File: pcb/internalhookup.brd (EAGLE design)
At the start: 29.6 x 16.9 mm, 8 parts, among them CN1 LASER, J1 CONTROL, J2 SERVO, J4 AZIMUTH, Q2 SMMBT2222ALT, U1 AMS1117-3.3

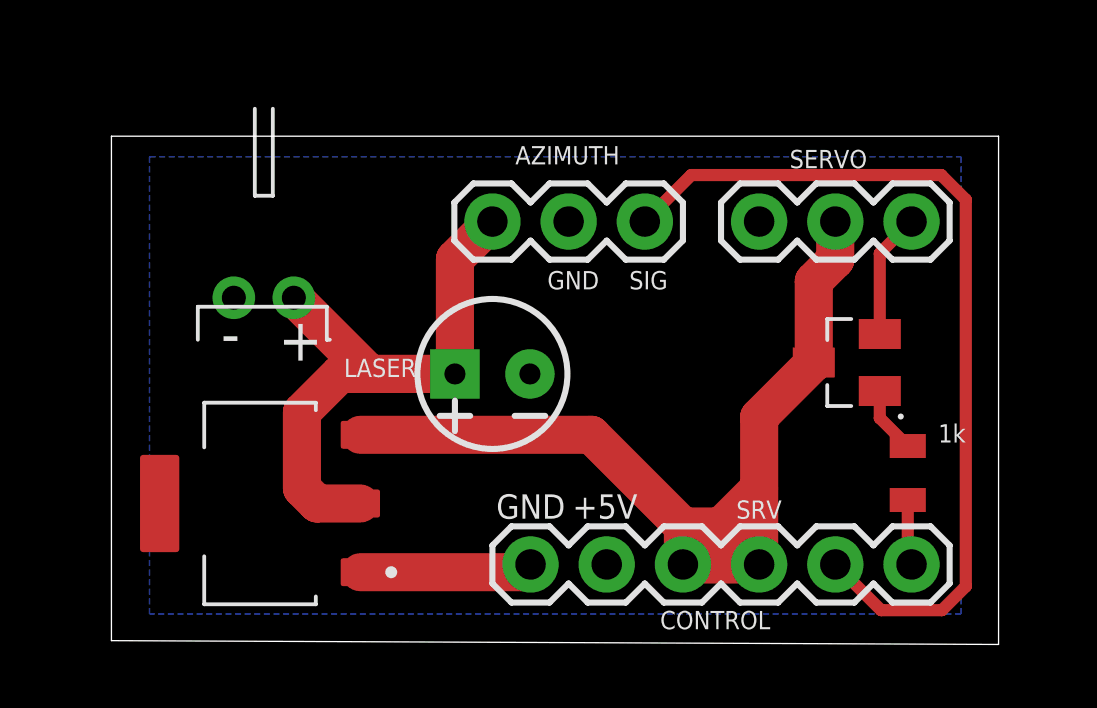
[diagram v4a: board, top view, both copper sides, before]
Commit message: PCB fixups
* Bumped PCB revisions
* Layout changes and some silk screen updates
* No functionality changes
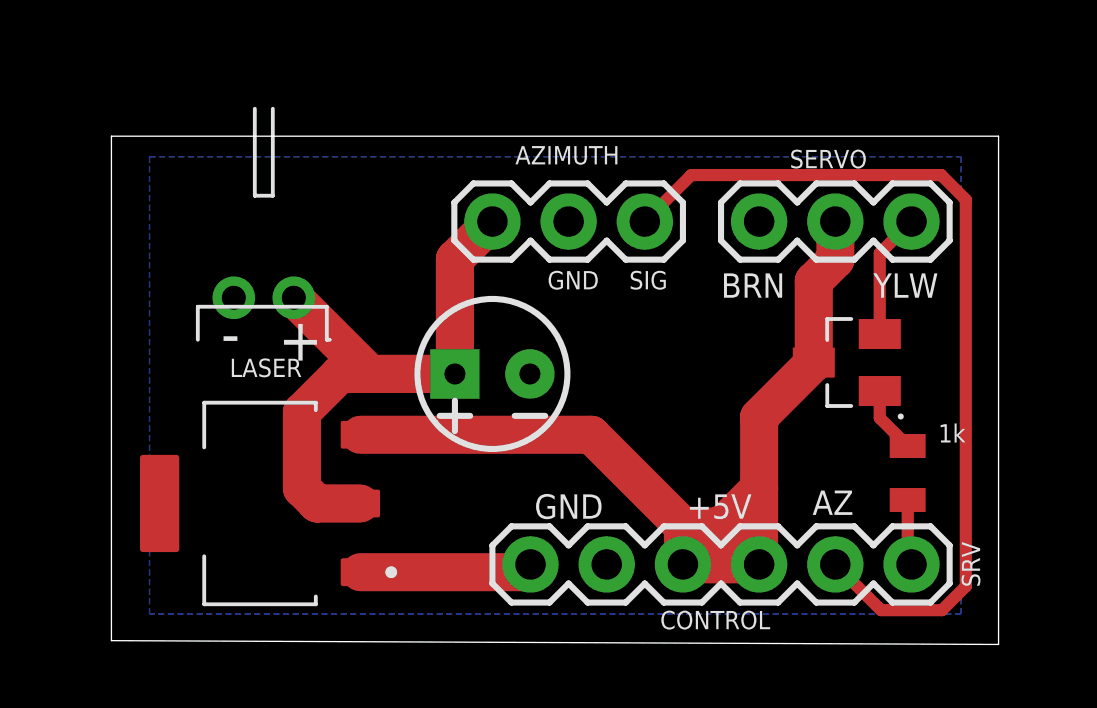
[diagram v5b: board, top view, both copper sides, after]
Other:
- board text added: "AZ"
- board text added: "BRN"
- board text added: "YLW"
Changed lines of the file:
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@@
 <wire x1="29.571" y1="16.815" x2="0" y2="16.815" width="0" layer="20"/>
 <wire x1="0" y1="16.815" x2="0" y2="0" width="0" layer="20"/>
-<text x="15.367" y="4.064" size="0.8128" layer="121">+5V</text>
-<text x="12.827" y="4.064" size="0.8128" layer="121">GND</text>
+<text x="19.177" y="4.064" size="0.8128" layer="121">+5V</text>
+<text x="14.097" y="4.064" size="0.8128" layer="121">GND</text>
 <text x="22.606" y="15.748" size="0.6096" layer="121">SERVO</text>
 <text x="18.288" y="0.381" size="0.6096" layer="121">CONTROL</text>
 <text x="27.559" y="6.604" size="0.6096" layer="121">1k</text>
-<text x="10.16" y="9.398" size="0.6096" layer="121" rot="R180">LASER</text>
+<text x="6.35" y="9.398" size="0.6096" layer="121" rot="R180">LASER</text>
 <text x="16.256" y="12.319" size="0.6096" layer="121" rot="R180">GND</text>
 <text x="18.542" y="12.319" size="0.6096" layer="121" rot="R180">SIG</text>
@@
 February 2021
 Version 1.4</text>
-<text x="20.828" y="4.064" size="0.6096" layer="121">SRV</text>
+<text x="28.956" y="1.778" size="0.6096" layer="121" rot="R90">SRV</text>
 <text x="13.462" y="15.875" size="0.6096" layer="121">AZIMUTH</text>
+<text x="23.368" y="4.191" size="0.8128" layer="121">AZ</text>
+<text x="20.32" y="11.43" size="0.8128" layer="121">BRN</text>
+<text x="25.4" y="11.43" size="0.8128" layer="121">YLW</text>
 </plain>
 <attributes>
@@
 <attribute name="PROD_ID" value="CONN-08437" x="26.67" y="2.54" size="0.8128" layer="27" rot="R180" display="off"/>
 </element>
-<element name="J4" library="SparkFun-Connectors" library_urn="urn:adsk.eagle:library:513" package="1X03" package3d_urn="urn:adsk.eagle:package:38063/1" value="AZIMUTH" x="12.7" y="13.97" smashed="yes">
-<attribute name="VALUE" x="11.43" y="11.938" size="0.6096" layer="27" font="vector" ratio="20"/>
-</element>
+<element name="J4" library="SparkFun-Connectors" library_urn="urn:adsk.eagle:library:513" package="1X03" package3d_urn="urn:adsk.eagle:package:38063/1" value="AZIMUTH" x="12.7" y="13.97" smashed="yes"/>
 </elements>
 <signals>

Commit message: Hookup board revision to 1.6
* Added a cap in front of the servo as the line to get the 5V is long
and may not be totally reliable under stress
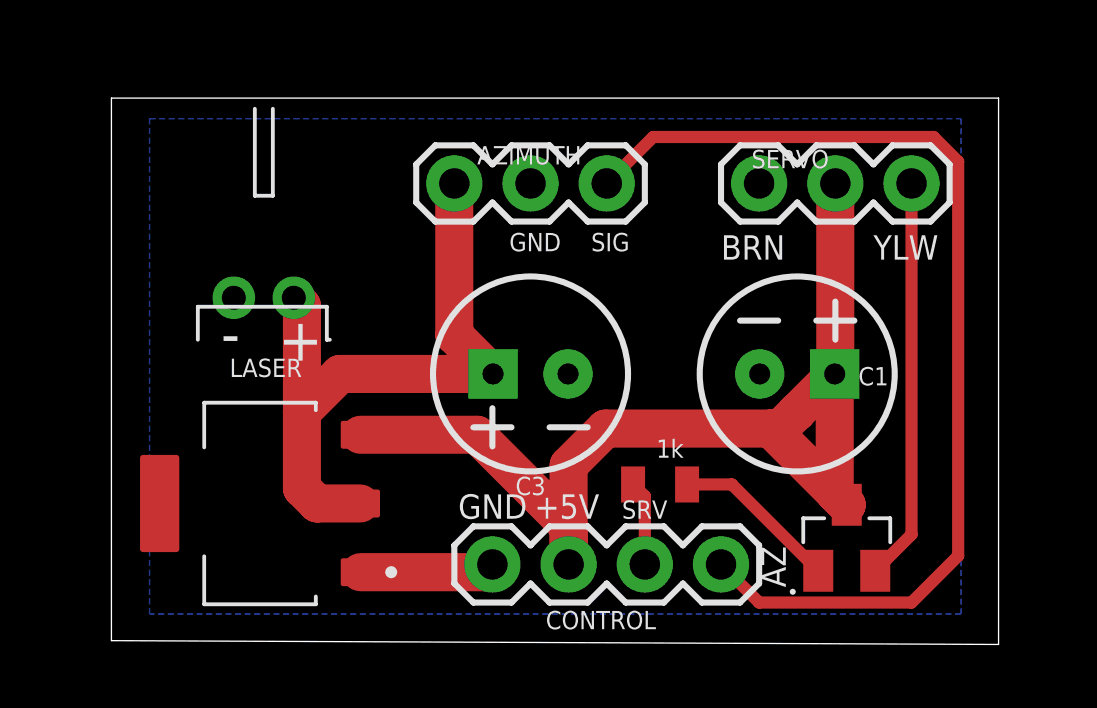
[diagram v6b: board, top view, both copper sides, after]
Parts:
- removed C2: 10uF, SparkFun-Capacitors:CPOL-RADIAL-2.5MM-5MM
- removed J1: CONTROL, SparkFun-Connectors:1X06
- added C1, C3: 100uF, SparkFun-Capacitors:CPOL-RADIAL-2.5MM-6.5MM
- added J3: CONTROL, SparkFun-Connectors:1X04
- moved R1 8.26 mm to (18.3, 5.21), turned to 0 degrees
- moved Q2 5.84 mm to (24.5, 3.43), turned to 0 degrees
- moved J4 1.80 mm to (11.4, 15.2)
- moved J2 1.27 mm to (21.6, 15.2)
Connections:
- net +3V3: now also C3.1; no longer C2.1
- net +5V: now also C1.1, J3.3; no longer J1.3, J1.4
- net AZIMUTH: now also J3.1; no longer J1.2
- net GND: now also C1.2, C3.2, J3.4; no longer C2.2, J1.5, J1.6
- net SERVO: now also J3.2; no longer J1.1
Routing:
- net N$2: track 4.19 -> 13.4 mm
- net AZIMUTH: track 29.9 -> 34.9 mm
- net +5V: track 32.6 -> 37.4 mm
- net N$1: track 2.22 -> 5.57 mm
- net GND: track 5.78 -> 4.51 mm
- net SERVO: track 2.20 -> 2.83 mm
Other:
- board size 29.6 x 16.9 mm -> 29.6 x 18.2 mm
- board text added: "ISS Control (C) Peter Buelow February 2021 Version 1.6"
- board text removed: "ISS Control (C) Peter Buelow February 2021 Version 1.4"

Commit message: Layout tweaks
* Swap pth for smd LED's
* Move globe power pin to new location
* Add support hole for motor board if attached via headers
* Layout fixes for globe with new 4 pin setup
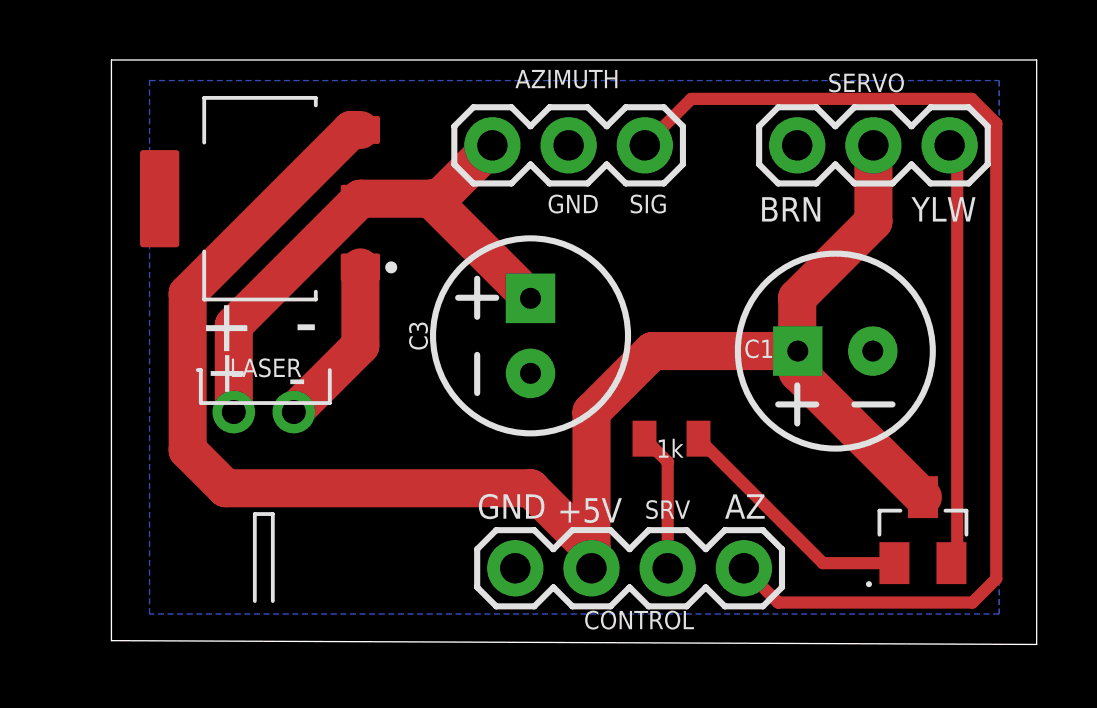
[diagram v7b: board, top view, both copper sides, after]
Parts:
- moved U1 10.2 mm to (4.95, 14.7)
- moved CN1 3.81 mm to (5.08, 7.62), turned to 180 degrees
- moved Q2 2.55 mm to (27.1, 3.68)
- moved J2 1.80 mm to (22.9, 16.5)
- moved J4 1.80 mm to (12.7, 16.5)
- moved R1 1.57 mm to (18.7, 6.73)
- moved C1 1.48 mm to (24.1, 9.65), turned to 180 degrees
- moved C3 1.27 mm to (14.0, 10.2), turned to 90 degrees
- moved J3 0.77 mm to (21.1, 2.41)
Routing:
- net +5V: track 37.4 -> 56.1 mm
- net +3V3: track 22.4 -> 18.7 mm
- net N$1: track 5.57 -> 8.25 mm
- net AZIMUTH: track 34.9 -> 37.1 mm
- net SERVO: track 2.83 -> 4.64 mm
- net GND: track 4.51 -> 5.74 mm
- net N$2: track 13.4 -> 14.1 mm
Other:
- board size 29.6 x 18.2 mm -> 30.8 x 19.5 mm
- board text added: "+"
- board text added: "-"
- board text added: "ISS Control (C) Peter Buelow February 2021 Version 1.8"
- board text removed: "ISS Control (C) Peter Buelow February 2021 Version 1.6"
